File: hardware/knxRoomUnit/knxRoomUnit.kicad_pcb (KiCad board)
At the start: 2 copper layers, 65 x 42 mm, 69 parts, among them J1 PROG, J2 KNX, P1 ePaper FL, P2 ePaper, Q1 S8050, Q2 S8050, Q3 SI1308, SW1 RESET, SW2 KNX, SW3 DW, SW4 OK, SW5 UP, U1 ESP32-WROOM-32, U2 SHT31-DIS, U3 VCNL4040M3OE

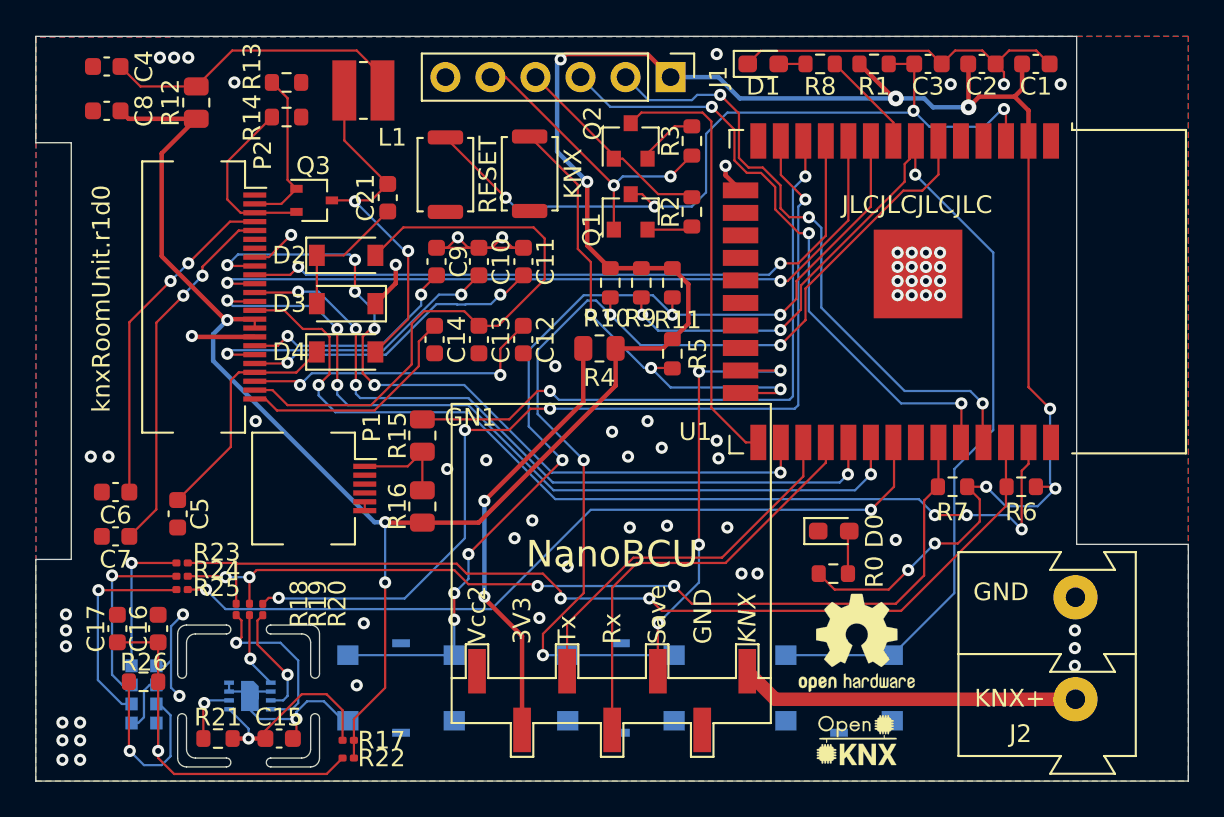
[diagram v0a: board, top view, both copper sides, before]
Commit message: Updated HW design
Flipped P1 to match display's pinout
Changed 0201 resistors to 0603
Added R12 to section 3V3 to display
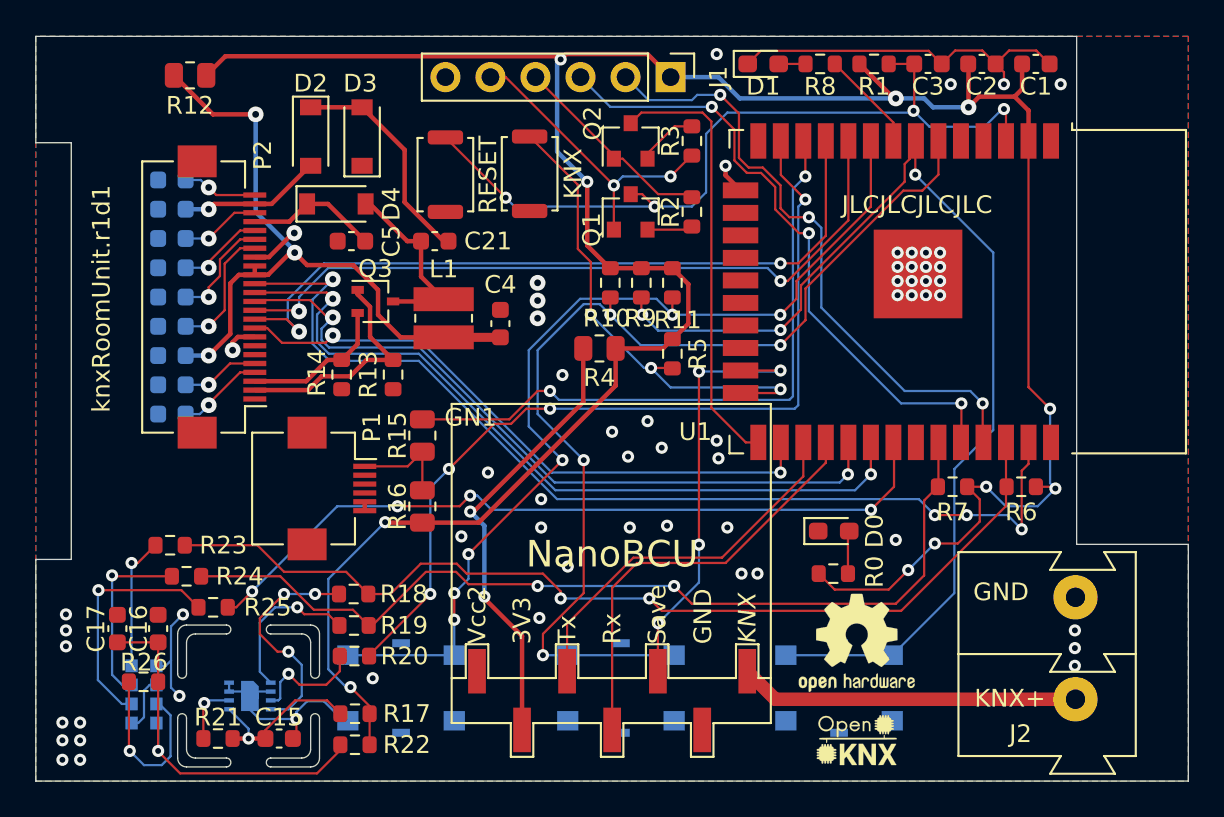
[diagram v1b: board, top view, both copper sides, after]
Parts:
- C10, C11, C12, C13, C14, C6, C7, C8, C9: moved to B.Cu
- R17, R18, R19, R20, R22, R23, R24, R25: footprint Resistor_SMD:R_0201_0603Metric -> Resistor_SMD:R_0603_1608Metric
- moved C4 26.5 mm to (114.2, 53.0), turned to 90 degrees
- moved C12 20.6 mm to (95.7, 48.2), turned to 180 degrees
- moved C11 19.8 mm to (95.7, 49.9), turned to 180 degrees
- moved C13 18.8 mm to (95.7, 46.6), turned to 180 degrees
- moved C5 18.2 mm to (105.8, 48.4), turned to 180 degrees
- moved R13 17.5 mm to (108.2, 55.9), turned to -90 degrees
- moved C10 17.4 mm to (95.7, 51.5), turned to 180 degrees
- moved C14 17.3 mm to (95.7, 44.9), turned to 180 degrees
- moved C9 15.4 mm to (95.7, 53.2), turned to 180 degrees
- moved R14 14.9 mm to (105.2, 55.9), turned to -90 degrees
- moved C8 14.3 mm to (95.7, 54.8)
- moved L1 13.6 mm to (111.0, 52.7), turned to 90 degrees
- moved D3 9.47 mm to (106.4, 42.5), turned to 90 degrees
- moved C7 9.12 mm to (95.7, 56.5)
- moved D4 8.37 mm to (105.0, 46.2)
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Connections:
- C4 pad 1: Net-(C4-Pad1) -> +3.3VA
- C8 pad 1: +3V3 -> +3.3VA
- L1 pad 1: Net-(C4-Pad1) -> +3.3VA
- P2 pad 15: +3V3 -> +3.3VA
- P2 pad 16: +3V3 -> +3.3VA
- R12 pad 2: Net-(C4-Pad1) -> +3.3VA
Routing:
- net +3.3VA: track 0.00 -> 39.4 mm, vias 0 -> 3
- net /ePaper/PREVGL: track 34.6 -> 8.16 mm, vias 0 -> 1
- net Net-(C4-Pad1): track 17.5 -> 0.00 mm
- net Net-(P2-Pin_5): track 20.7 -> 4.45 mm, vias 2 -> 1
- net GND: track 60.4 -> 45.4 mm, vias 69 -> 61
- net +3V3: track 171.4 -> 156.5 mm, vias 12 -> 11
- net Net-(P2-Pin_4): track 19.0 -> 4.93 mm, vias 2 -> 1
- net Net-(P2-Pin_22): track 17.8 -> 4.50 mm, vias 2 -> 1
- net Net-(P2-Pin_20): track 17.5 -> 4.96 mm, vias 2 -> 1
- net Net-(P2-Pin_19): track 17.7 -> 6.11 mm, vias 2 -> 1
- net Net-(D4-A): track 20.6 -> 10.9 mm, vias 2 -> 0
- net EPAPER_BUSY: track 44.2 -> 35.1 mm, vias 6 -> 2
- net Net-(P2-Pin_24): track 13.2 -> 4.25 mm, vias 0 -> 1
- net /ePaper/PREVGH: track 13.5 -> 7.51 mm
- net Net-(P2-Pin_18): track 12.8 -> 7.26 mm, vias 2 -> 1
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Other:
- board text added: "knxRoomUnit.r1d1"
- board text removed: "knxRoomUnit.r1d0"
